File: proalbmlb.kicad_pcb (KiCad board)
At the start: 4 copper layers, 24.4 x 35.8 mm, 47 parts, among them J1 DE9_Pins_MountingHoles, J10 Conn_01x08_Socket, J11 Conn_01x08_Socket, J2 Conn_01x08_Socket, J3 HPF-02-01-X-S, J4 Conn_01x04_Socket, J5 Conn_01x04_Socket, J6 Conn_01x04_Socket, J7 Conn_01x04_Socket, J8 Conn_01x02_Pin, J9 Conn_01x02_Pin, SW1 SW_DPST, SW2 SW_Rotary_1x3_MP, SW3 SW_Push_LED, U10 PTMUX6236RUMR, U11 TMUX7219MDGKR, U12 PTMUX6236RUMR, U2 SC1176, U3 TMUX7201RQXR, U7 PINA745AIRELR, U8 PTMUX6236RUMR, U9 PINA745AIRELR

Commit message: board modify
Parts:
- removed U2: SC1176, pictures:MODULE_SC1176
- added REF**: Raspberry_Pi_Zero_Socketed_THT_FaceDown_MountingHoles, Module:Raspberry_Pi_Zero_Socketed_THT_FaceDown_MountingHoles, F.Cu at (124.2, 74.5)
- J11, J5, J7, J9: moved to B.Cu
- J2: footprint Connector_PinHeader_2.54mm:PinHeader_1x08_P2.54mm_Vertical -> Connector_PinSocket_2.54mm:PinSocket_1x08_P2.54mm_Vertical
- SW1: footprint Button_Switch_THT:SW_NKK_G1xJP -> Button_Switch_THT:Untitled
- SW2: footprint Button_Switch_THT:A_D22022LB -> Button_Switch_THT:AA_CPA_10
- U10, U8: footprint PTMUX6236RUMR:WQFN16_RUM_TEX -> Package_DFN_QFN:WQFN-16-1EP_4x4mm_P0.5mm_EP2.6x2.6mm_ThermalVias
- moved J8 269.4 mm to (118.3, 85.3)
- moved J7 254.2 mm to (168.6, 124.8), turned to -90 degrees
- moved J9 253.2 mm to (128.5, 118.0), turned to 180 degrees
- moved J10 249.0 mm to (133.7, 84.3)
- moved J6 245.9 mm to (166.4, 110.8)
- moved C28 240.8 mm to (160.5, 91.0)
- moved C29 240.8 mm to (160.5, 92.4)
- moved C25 240.8 mm to (154.8, 87.3)
- moved C26 240.8 mm to (163.1, 84.4)
- moved C27 240.8 mm to (153.3, 87.3)
- moved U10 240.8 mm to (158.2, 86.0)
- moved C24 240.8 mm to (161.6, 84.4)
- moved C30 240.8 mm to (169.4, 89.6)
- moved C31 240.8 mm to (167.9, 89.6)
- moved U11 240.8 mm to (164.0, 88.8)
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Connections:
- C3 pad 2: VDD -> Net-(U8-VSS)
- C4 pad 2: VDD -> Net-(U8-VSS)
- U1 pad 4: unconnected-(U1-SDA_3V3-Pad4) -> /Project Architecture/Connectors/SDA
- U1 pad 5: /Project Architecture/Connectors/SDA -> /Project Architecture/Connectors/SDC
- U10 pad 10: /Project Architecture/Connectors/J1_3 -> /Project Architecture/Connectors/J1_7
- U10 pad 16: /Project Architecture/Connectors/J1_2 -> /Project Architecture/Connectors/J1_6
- U10 pad 2: /Project Architecture/Connectors/J1_1 -> /Project Architecture/Connectors/J1_5
- U12 pad 17: unconnected-(U12-EPAD-Pad17)_5 -> GND
- U3 pad 9: unconnected-(U3-NC/GND-Pad9) -> GND
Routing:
- net /Project Architecture/Connectors/Stow: track 0.00 -> 95.2 mm
- net /Project Architecture/Connectors/SDA: track 0.00 -> 81.8 mm, vias 2 -> 1
- net /Project Architecture/Connectors/SDC: track 0.00 -> 80.5 mm
- net /Project Architecture/Raspberrypi/PWM: track 0.00 -> 43.1 mm, vias 0 -> 1
- net /Project Architecture/Connectors/J1_6: track 0.00 -> 40.5 mm, vias 0 -> 1
- net /Project Architecture/Connectors/J1_5: track 0.00 -> 31.8 mm, vias 0 -> 1
- net /Project Architecture/Connectors/J1_7: track 0.00 -> 28.6 mm
- net /Project Architecture/Connectors/SFF: track 0.00 -> 27.2 mm
- net /Project Architecture/Motor Polarity Switch/+M: track 20.4 -> 2.70 mm, vias 3 -> 0
- net /Project Architecture/MotorB/-MB: track 17.2 -> 1.17 mm
- net /Project Architecture/Connectors/J1_8: track 6.43 -> 18.7 mm, vias 1 -> 0
- net /Project Architecture/Connectors/J1_9: track 3.33 -> 14.6 mm, vias 1 -> 0
- net /Project Architecture/Connectors/RE1.A: track 0.00 -> 10.5 mm
- net /Project Architecture/MotorB/+MB: track 5.18 -> 15.1 mm, vias 1 -> 2
- net /Project Architecture/Connectors/RE2.C: track 0.00 -> 9.19 mm
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- added copper zone on F.Cu, net (none)
- added copper zone on B.Cu, net +5V
- added copper zone on F.Cu, net +5V
- added copper zone on In1.Cu, net +5V
- added copper zone on F.Cu, net /Project Architecture/ALB-MLB Toggle/+M
- added copper zone on B.Cu, net /Project Architecture/ALB-MLB Toggle/+MB
- added copper zone on F.Cu, net /Project Architecture/ALB-MLB Toggle/-M
- added copper zone on In1.Cu, net /Project Architecture/ALB-MLB Toggle/-M
- added copper zone on In2.Cu, net /Project Architecture/ALB-MLB Toggle/-M
- added copper zone on In2.Cu, net /Project Architecture/Connectors/SFF
- added copper zone on B.Cu, net /Project Architecture/Connectors/Stow
- added copper zone on In1.Cu, net /Project Architecture/Motor Polarity Switch/+M
- added copper zone on F.Cu, net GND
- added copper zone on In1.Cu, net GND
- added copper zone on In2.Cu, net GND
- added copper zone on F.Cu, net Net-(U7-Pad1)
- added copper zone on F.Cu, net VDD
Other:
- board size 24.4 x 35.8 mm -> 93.8 x 92.5 mm

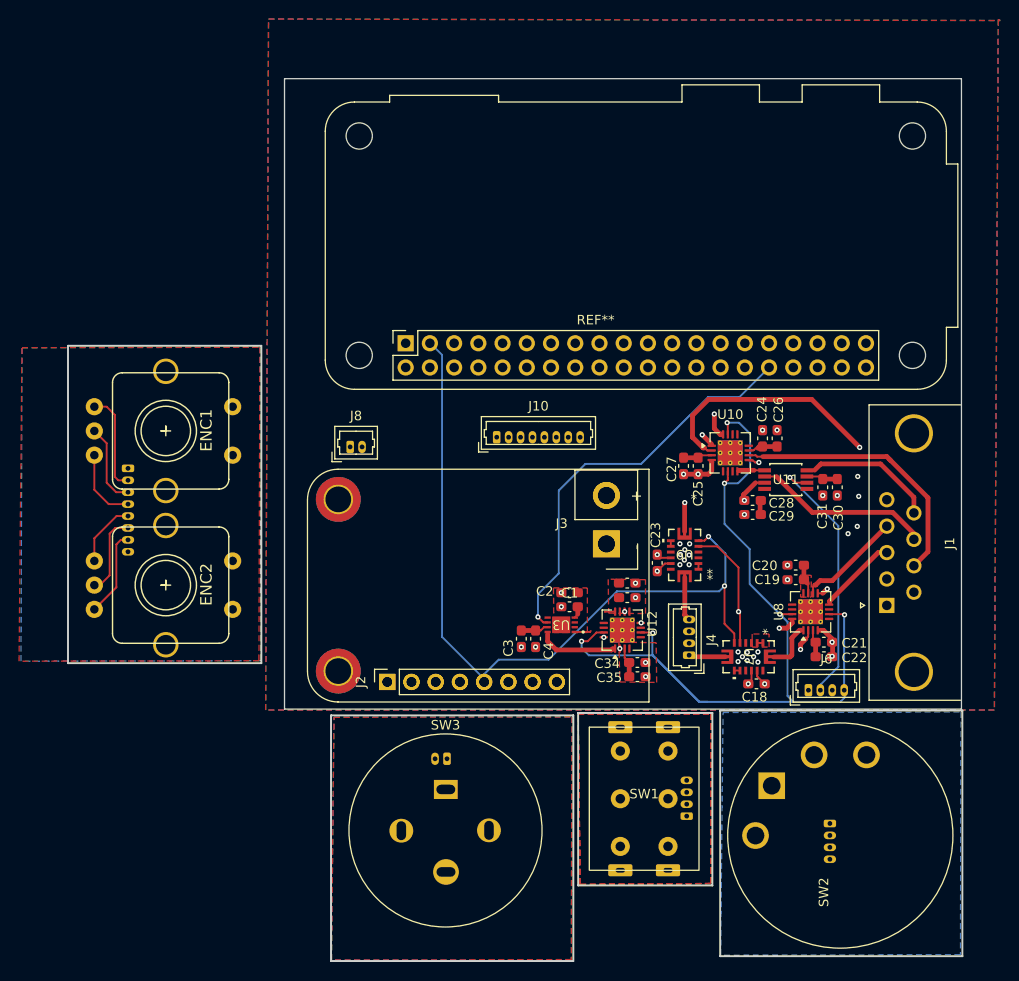
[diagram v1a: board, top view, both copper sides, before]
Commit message: added zones
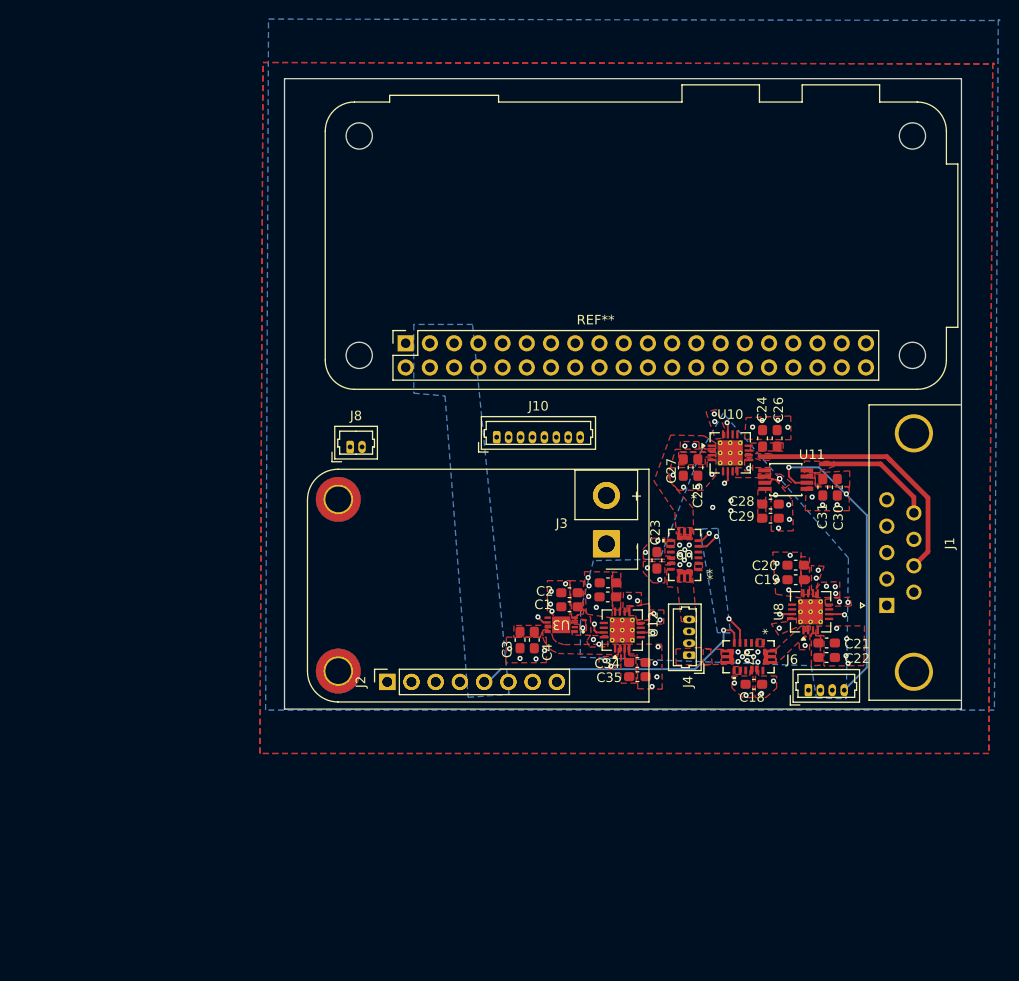
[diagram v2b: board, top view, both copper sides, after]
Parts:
- removed ENC1, ENC2: Encoder_Rotary_11mm_SPST_DShaft, PCM_4ms_Encoder:ROTENC-12MM-BUT
- removed J11: Conn_01x08_Socket, Connector_Molex:Molex_PicoBlade_53047-0810_1x08_P1.25mm_Vertical
- removed J5, J7: Conn_01x04_Socket, Connector_Molex:Molex_PicoBlade_53048-0410_1x04_P1.25mm_Horizontal
- removed J9: Conn_01x02_Pin, Connector_Molex:Molex_PicoBlade_53048-0210_1x02_P1.25mm_Horizontal
- removed SW1: SW_DPST, Button_Switch_THT:Untitled
- removed SW2: SW_Rotary_1x3_MP, Button_Switch_THT:AA_CPA_10
- removed SW3: SW_Push_LED, Button_Switch_THT:BH16NBSBB
- moved C33 2.05 mm to (145.3, 101.1), turned to 180 degrees
- moved C32 2.02 mm to (145.4, 99.6), turned to 180 degrees
- moved C29 1.92 mm to (162.4, 92.8), turned to 0 degrees
- moved C28 1.92 mm to (162.4, 91.3), turned to 0 degrees
- moved C21 0.30 mm to (168.3, 105.9)
- moved C22 0.30 mm to (168.3, 107.4)
- moved C18 0.28 mm to (160.7, 110.2)
- moved C23 0.27 mm to (150.5, 97.2)
- moved C3 0.19 mm to (136.1, 105.6)
- moved C4 0.19 mm to (137.6, 105.6)
- moved C25 0.17 mm to (154.8, 87.5)
- moved C27 0.17 mm to (153.3, 87.5)
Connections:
- J3 pad 1: (no net) -> GND
- J3 pad 2: (no net) -> VDD
- J4 pad 1: /Project Architecture/Connectors/+M -> /Project Architecture/Motor A/+M
- J4 pad 2: /Project Architecture/Connectors/-M -> /Project Architecture/Motor A/-M
- J4 pad 3: /Project Architecture/Connectors/-MB -> /Project Architecture/MotorB/-MB
- J4 pad 4: /Project Architecture/Connectors/+MB -> /Project Architecture/MotorB/+MB
- J6 pad 2: /Project Architecture/Connectors/SFF -> /Project Architecture/Connectors/Stow
- J6 pad 4: /Project Architecture/Connectors/Stow -> /Project Architecture/Connectors/SFF
- U12 pad : (no net) -> GND
- U12 pad 10: /Project Architecture/Motor Polarity Switch/-M -> /Project Architecture/Connectors/-M
- U12 pad 16: /Project Architecture/Motor Polarity Switch/+M -> /Project Architecture/Connectors/+M
- U12 pad 2: /Project Architecture/Motor Polarity Switch/+M -> /Project Architecture/Connectors/+M
- U12 pad 8: /Project Architecture/Motor Polarity Switch/-M -> /Project Architecture/Connectors/-M
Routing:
- net /Project Architecture/Connectors/Stow: track 95.2 -> 8.74 mm
- net /Project Architecture/Connectors/SDC: track 80.5 -> 32.3 mm
- net /Project Architecture/Connectors/SDA: track 81.8 -> 40.0 mm, vias 1 -> 2
- net +3.3V: track 0.00 -> 26.2 mm
- net /Project Architecture/Connectors/-MB: track 21.6 -> 0.00 mm
- net /Project Architecture/Motor A/-M: track 18.1 -> 0.00 mm, vias 1 -> 3
- net VDD: track 18.2 -> 0.59 mm, vias 4 -> 3
- net /Project Architecture/MotorB/+MB: track 15.1 -> 0.00 mm, vias 2 -> 0
- net GND: track 14.3 -> 0.07 mm, vias 38 -> 82
- net /Project Architecture/Raspberrypi/PWM: track 43.1 -> 30.0 mm
- net /Project Architecture/Connectors/J1_4: track 11.0 -> 0.00 mm, vias 0 -> 2
- net /Project Architecture/Connectors/RE1.A: track 10.5 -> 0.00 mm
- net /Project Architecture/Connectors/RE2.C: track 9.19 -> 0.00 mm
- net /Project Architecture/Motor A/+M: track 9.01 -> 0.22 mm
- net /Project Architecture/Connectors/-M: track 8.62 -> 0.00 mm, vias 2 -> 4
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- added copper zone on F.Cu, net +VDC
- added copper zone on F.Cu, net /Project Architecture/Connectors/+M
- added copper zone on In1.Cu, net /Project Architecture/Connectors/+M
- added copper zone on F.Cu, net /Project Architecture/Connectors/-M
- added copper zone on In1.Cu, net /Project Architecture/Connectors/-M
- added copper zone on F.Cu, net /Project Architecture/Connectors/J1_1
- added copper zone on F.Cu, net /Project Architecture/Connectors/J1_2
- added copper zone on F.Cu, net /Project Architecture/Connectors/J1_3
- added copper zone on In1.Cu, net /Project Architecture/Connectors/J1_3
- added copper zone on F.Cu, net /Project Architecture/Connectors/J1_4
- added copper zone on In1.Cu, net /Project Architecture/Connectors/J1_4
- added copper zone on F.Cu, net /Project Architecture/Connectors/J1_5
- added copper zone on In1.Cu, net /Project Architecture/Connectors/J1_5
- added copper zone on F.Cu, net /Project Architecture/Connectors/J1_6
- added copper zone on In1.Cu, net /Project Architecture/Connectors/J1_6
- added copper zone on F.Cu, net /Project Architecture/Connectors/J1_7
- added copper zone on F.Cu, net /Project Architecture/Connectors/J1_8
- added copper zone on F.Cu, net /Project Architecture/Connectors/J1_9
- added copper zone on In2.Cu, net /Project Architecture/Connectors/SDA
- added copper zone on B.Cu, net /Project Architecture/Connectors/SDC
- added copper zone on F.Cu, net /Project Architecture/Motor A/+M
- added copper zone on F.Cu, net /Project Architecture/Motor A/-M
- added copper zone on In1.Cu, net /Project Architecture/Motor A/-M
- added copper zone on F.Cu, net /Project Architecture/MotorB/+MB
- added copper zone on F.Cu, net /Project Architecture/MotorB/-MB
- added copper zone on In1.Cu, net /Project Architecture/MotorB/-MB
- added copper zone on F.Cu, net /Project Architecture/MotorB/J1_[8..9]
- added copper zone on In2.Cu, net /Project Architecture/Raspberrypi/PWM
- added copper zone on F.Cu, net Net-(U10-VSS)
- added copper zone on F.Cu, net Net-(U11-VSS)
- added copper zone on F.Cu, net Net-(U12-VSS)
- added copper zone on F.Cu, net Net-(U7-Pad8)
- added copper zone on F.Cu, net Net-(U8-VSS)
- added copper zone on F.Cu, net Net-(U9-Pad1)
- added copper zone on F.Cu, net Net-(U9-Pad8)
- added copper zone on In2.Cu, net VDD
- removed copper zone on F.Cu, net (none)
- removed copper zone on In1.Cu, net +5V
- removed copper zone on F.Cu, net /Project Architecture/ALB-MLB Toggle/+M
- removed copper zone on B.Cu, net /Project Architecture/ALB-MLB Toggle/+MB
- removed copper zone on F.Cu, net /Project Architecture/ALB-MLB Toggle/-M
- removed copper zone on In1.Cu, net /Project Architecture/ALB-MLB Toggle/-M
- removed copper zone on In2.Cu, net /Project Architecture/ALB-MLB Toggle/-M
- removed copper zone on In2.Cu, net /Project Architecture/Connectors/SFF
- removed copper zone on In1.Cu, net /Project Architecture/Motor Polarity Switch/+M
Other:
- board size 93.8 x 92.5 mm -> 71 x 66.1 mm

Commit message: dimensions
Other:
- board text removed: "30°"
